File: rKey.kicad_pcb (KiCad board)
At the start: 2 copper layers, 52.8 x 71.4 mm, 39 parts, among them IC1 BDX34C, J1 Conn_01x06, Q1 BC337, Q2 BC337, Q3 BC337, Q4 BC337, Q5 BC327, Q8 BC337, U1 TL084BCN, U2 LM7810_TO220

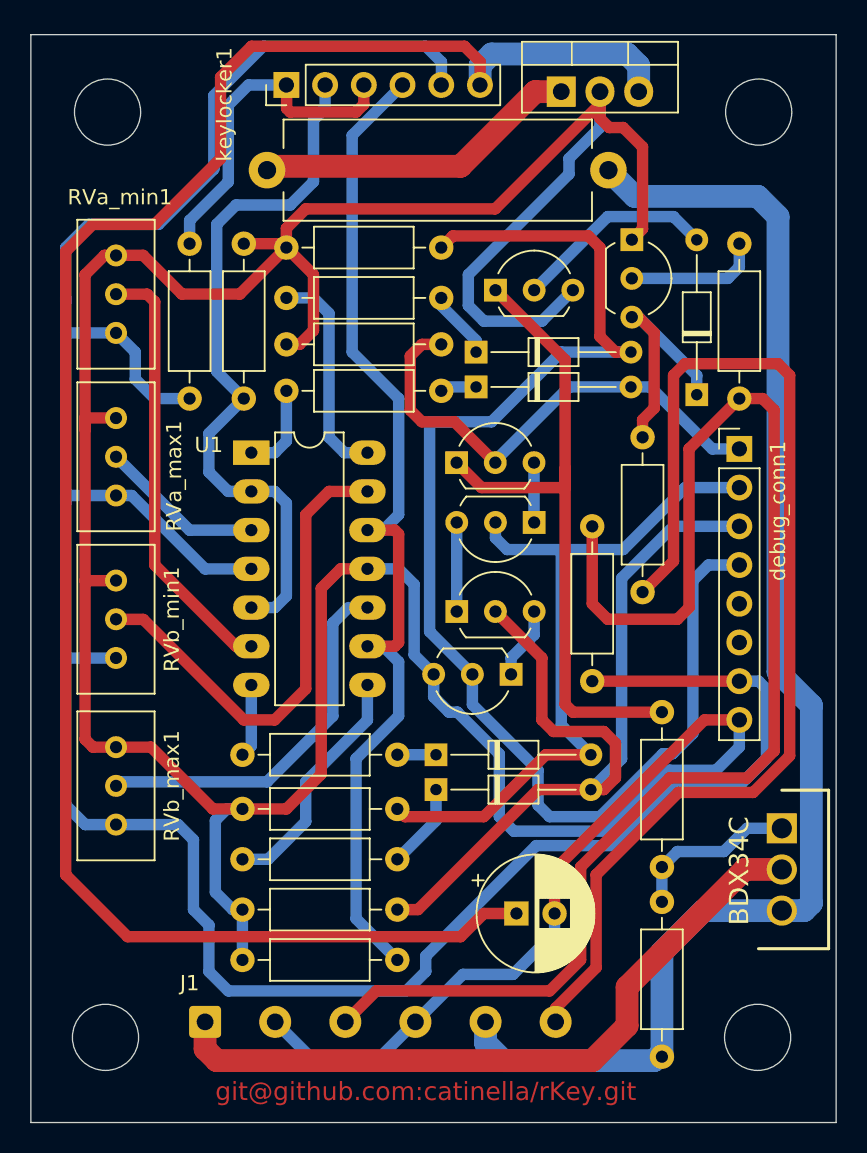
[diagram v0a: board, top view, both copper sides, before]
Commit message: feat: Locking the engine when the vehicle is off
In order to forbid to manually run the engine when the vehicle is off, I added a NC micro relay.
PCB size has been reduced
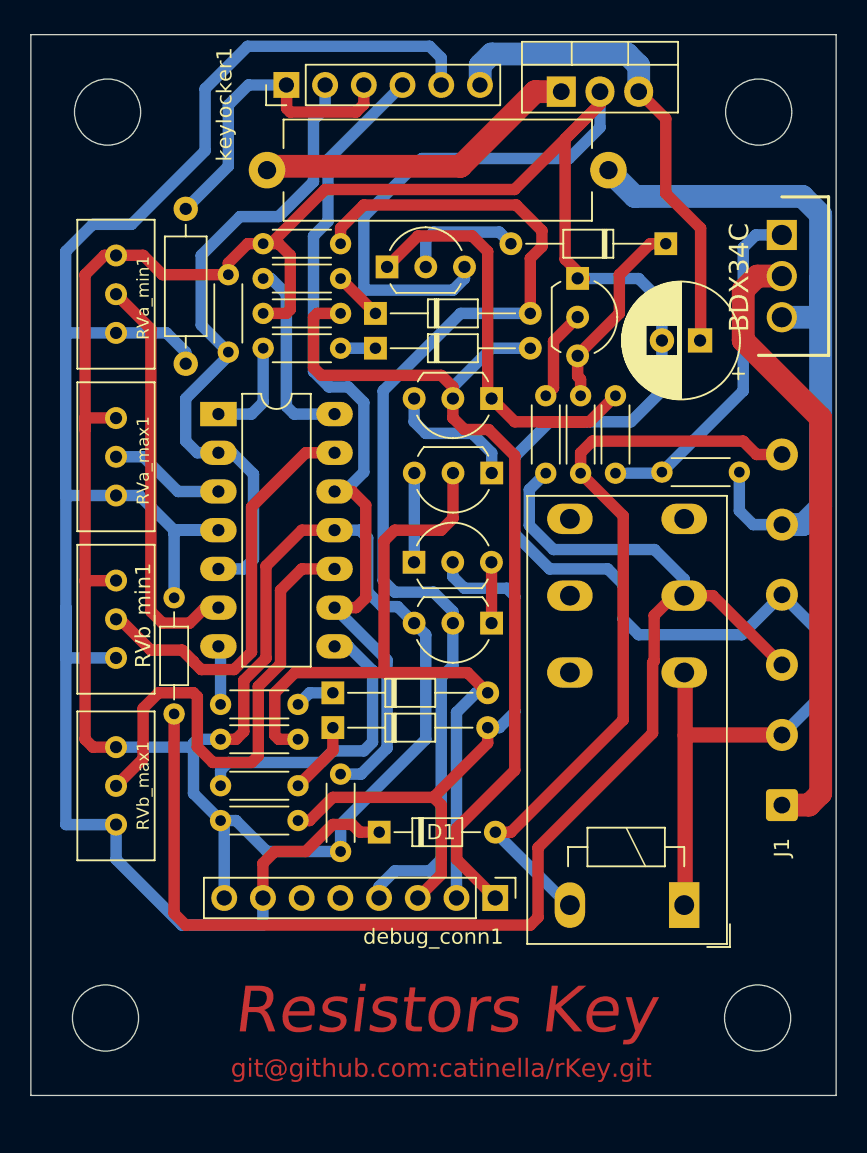
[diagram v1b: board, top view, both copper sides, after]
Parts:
- added D1: DIODE, Diode_THT:D_DO-34_SOD68_P7.62mm_Horizontal, F.Cu at (139.4, 109.0)
- added K1: RT42xxxx, Relay_THT:Relay_DPDT_Schrack-RT2-FormC_RM5mm, F.Cu at (159.5, 113.8)
- R10, R11, R12, R13, R15, R16, R17, R2, R3, R4, R5, R7, R8, R9: footprint Resistor_THT:R_Axial_DIN0207_L6.3mm_D2.5mm_P10.16mm_Horizontal -> Resistor_THT:R_Axial_DIN0204_L3.6mm_D1.6mm_P5.08mm_Horizontal
- R14: footprint Resistor_THT:R_Axial_DIN0207_L6.3mm_D2.5mm_P10.16mm_Horizontal -> Resistor_THT:R_Axial_DIN0204_L3.6mm_D1.6mm_P7.62mm_Horizontal
- moved J1 40.4 mm to (165.9, 107.2), turned to 90 degrees
- moved C1 39.5 mm to (160.5, 76.7), turned to 180 degrees
- moved IC1 38.9 mm to (165.9, 69.8)
- moved debug_conn1 33.5 mm to (147.1, 113.3), turned to -90 degrees
- moved R11 28.2 mm to (158.0, 85.3), turned to 0 degrees
- moved R14 28.0 mm to (126.0, 93.6), turned to -90 degrees
- moved R10 21.0 mm to (154.9, 80.3)
- moved R13 16.1 mm to (150.4, 80.3)
- moved R8 12.7 mm to (136.9, 105.2), turned to -90 degrees
- moved ZD1 10.1 mm to (158.2, 70.4), turned to 180 degrees
- moved ZD2 7.90 mm to (136.4, 99.8)
- moved ZD3 7.90 mm to (136.4, 102.1)
- moved Q8 7.27 mm to (140.0, 71.9)
- moved ZD5 7.08 mm to (139.2, 77.2)
- moved ZD4 7.08 mm to (139.2, 74.9)
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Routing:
- net Net-(U2-Pad3): track 124.1 -> 31.8 mm
- net Net-(R1-Pad1): track 179.0 -> 136.1 mm
- net Net-(IC1-Pad3): track 89.7 -> 48.1 mm
- net GND: track 256.8 -> 289.2 mm
- net Net-(Q1-Pad2): track 32.7 -> 60.5 mm
- net Net-(K1-PadA2): track 75.0 -> 50.8 mm
- net Net-(Q3-Pad2): track 57.8 -> 38.4 mm
- net Net-(Q4-Pad2): track 88.8 -> 73.1 mm
- net Net-(Q1-Pad1): track 44.7 -> 30.1 mm
- net Net-(IC1-Pad1): track 10.7 -> 22.1 mm
- net Net-(R8-Pad1): track 69.0 -> 57.6 mm
- net Net-(RVb_max1-Pad2): track 23.7 -> 33.8 mm
- net Net-(IC1-Pad2): track 46.6 -> 40.9 mm
- net Net-(Q8-Pad2): track 13.3 -> 7.89 mm
- net Net-(Q1-Pad3): track 3.93 -> 8.78 mm
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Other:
- board size 52.8 x 71.4 mm -> 52.8 x 69.6 mm
- board text added: "Resistors Key"

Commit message: small fixes...
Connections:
- J1 pad 3: Net-(K1-Pad11) -> Net-(J1-Pad3)
- K1 pad 11: Net-(K1-Pad11) -> Net-(J1-Pad3)
- K1 pad 21: unconnected-(K1-Pad21) -> Net-(J1-Pad3)
- K1 pad 22: unconnected-(K1-Pad22) -> GND
- R13 pad 2: Net-(K1-Pad11) -> Net-(J1-Pad3)
- R14 pad 2: Net-(K1-Pad11) -> Net-(J1-Pad3)
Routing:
- net Net-(J1-Pad3): track 0.00 -> 88.1 mm
- net Net-(K1-Pad11): track 87.9 -> 0.00 mm
- net GND: track 289.2 -> 293.8 mm

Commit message: fixes
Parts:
- removed D1: DIODE, Diode_THT:D_DO-34_SOD68_P7.62mm_Horizontal
- added C2: 150uF, Capacitor_THT:CP_Radial_D7.5mm_P2.50mm, F.Cu at (131.1, 121.6)
- added Q6: BC327, Package_TO_SOT_THT:TO-92L_Inline_Wide, F.Cu at (151.6, 118.6)
- added Q7: BC337, Package_TO_SOT_THT:TO-92L_Inline_Wide, F.Cu at (138.2, 121.9)
- added Q9: BC327, Package_TO_SOT_THT:TO-92L_Inline_Wide, F.Cu at (153.9, 119.6)
- added R18: 50K, Resistor_THT:R_Axial_DIN0204_L3.6mm_D1.6mm_P5.08mm_Horizontal, F.Cu at (136.4, 125.0)
- added R19: 20K, Resistor_THT:R_Axial_DIN0204_L3.6mm_D1.6mm_P5.08mm_Horizontal, F.Cu at (149.1, 125.0)
- added R20: 20K, Resistor_THT:R_Axial_DIN0204_L3.6mm_D1.6mm_P5.08mm_Horizontal, F.Cu at (151.4, 125.0)
- added R21: 200K, Resistor_THT:R_Axial_DIN0204_L3.6mm_D1.6mm_P5.08mm_Horizontal, F.Cu at (138.2, 117.9)
- added R22: 10K, Resistor_THT:R_Axial_DIN0204_L3.6mm_D1.6mm_P5.08mm_Horizontal, F.Cu at (156.5, 122.7)
- moved J1 4.81 mm to (164.6, 111.8)
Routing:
- net Net-(R14-Pad1): track 136.1 -> 164.9 mm
- net Net-(C2-Pad1): track 0.00 -> 22.9 mm
- net Net-(R13-Pad2): track 88.1 -> 109.5 mm
- net Net-(Q7-Pad1): track 0.00 -> 15.3 mm
- net Net-(J1-Pad6): track 50.8 -> 61.6 mm
- net Net-(Q9-Pad3): track 0.00 -> 6.44 mm
- net Net-(Q6-Pad2): track 0.00 -> 6.35 mm
- net Net-(IC1-Pad2): track 40.9 -> 46.6 mm
- net Net-(IC1-Pad3): track 48.1 -> 51.9 mm
- net Net-(Q7-Pad2): track 0.00 -> 3.43 mm
- net Net-(R10-Pad1): track 30.1 -> 26.8 mm
- net Net-(Q9-Pad2): track 0.00 -> 3.11 mm
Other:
- board text removed: "Resistors Key"

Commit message: fix
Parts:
- removed R6: 20, Resistor_THT:R_Axial_Power_L20.0mm_W6.4mm_P22.40mm
- R1: footprint Resistor_THT:R_Axial_DIN0207_L6.3mm_D2.5mm_P10.16mm_Horizontal -> Resistor_THT:R_Axial_Power_L20.0mm_W6.4mm_P22.40mm
- U2: value LM7810_TO220 -> LM7810
- moved R1 28.0 mm to (151.7, 65.5), turned to 180 degrees
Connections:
- IC1 pad 3: Net-(IC1-Pad3) -> Net-(U2-Pad1)
- J1 pad 5: Net-(IC1-Pad3) -> Net-(U2-Pad1)
- R11 pad 2: Net-(IC1-Pad3) -> Net-(U2-Pad1)
- U2 pad 1: Net-(R6-Pad1) -> Net-(U2-Pad1)
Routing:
- net Net-(U2-Pad1): track 0.00 -> 57.6 mm
- net Net-(IC1-Pad3): track 51.9 -> 0.00 mm
- net GND: track 293.7 -> 272.0 mm, vias 0 -> 1
- net Net-(R6-Pad1): track 21.4 -> 0.00 mm
- net Net-(Q6-Pad3): track 164.9 -> 172.8 mm
- net Net-(R1-Pad2): track 20.8 -> 17.2 mm

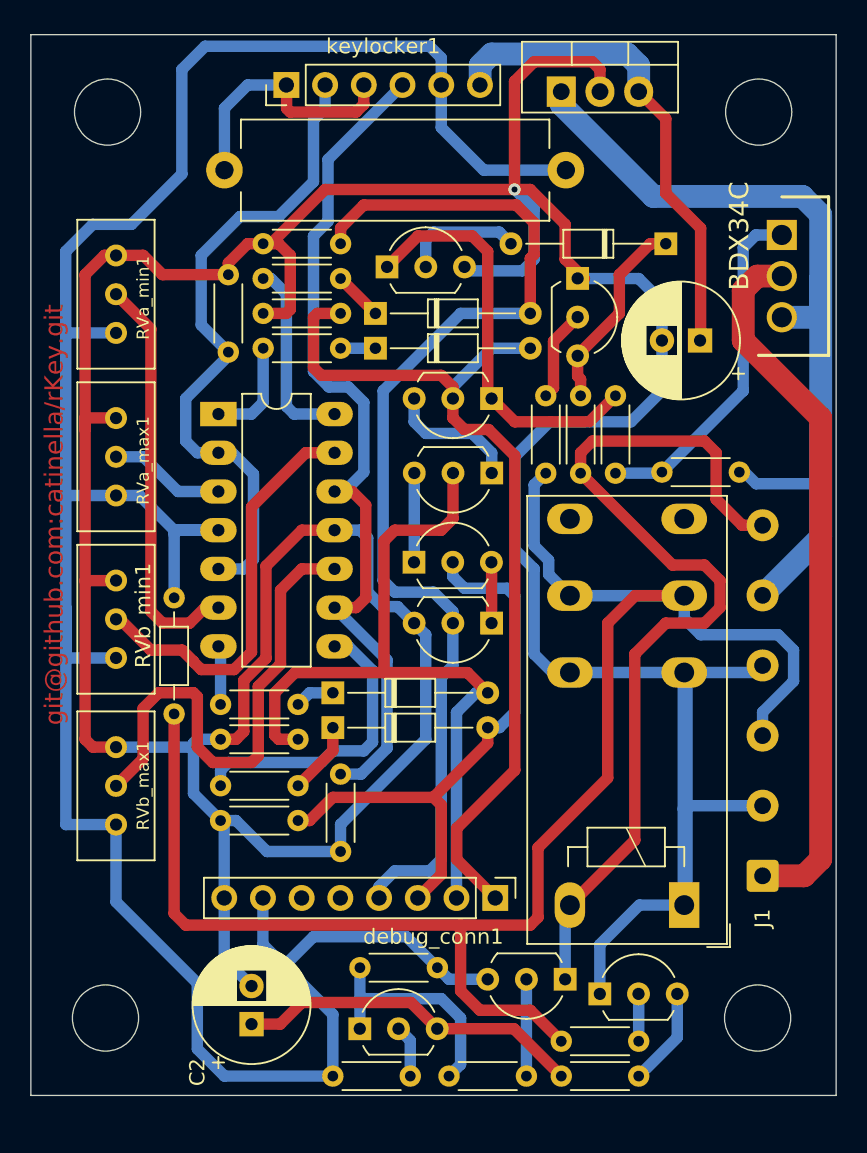
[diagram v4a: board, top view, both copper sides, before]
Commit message: Enhancements and fixes
1) the generic rerlay has been replaced by HK19F
2) unuseful components have been removed
3) pull-down resistors resizing from 8K to more common 10K
4) the 12K resistor linked to the BC237 IC's emiotter, has been resized from 12K to 6K
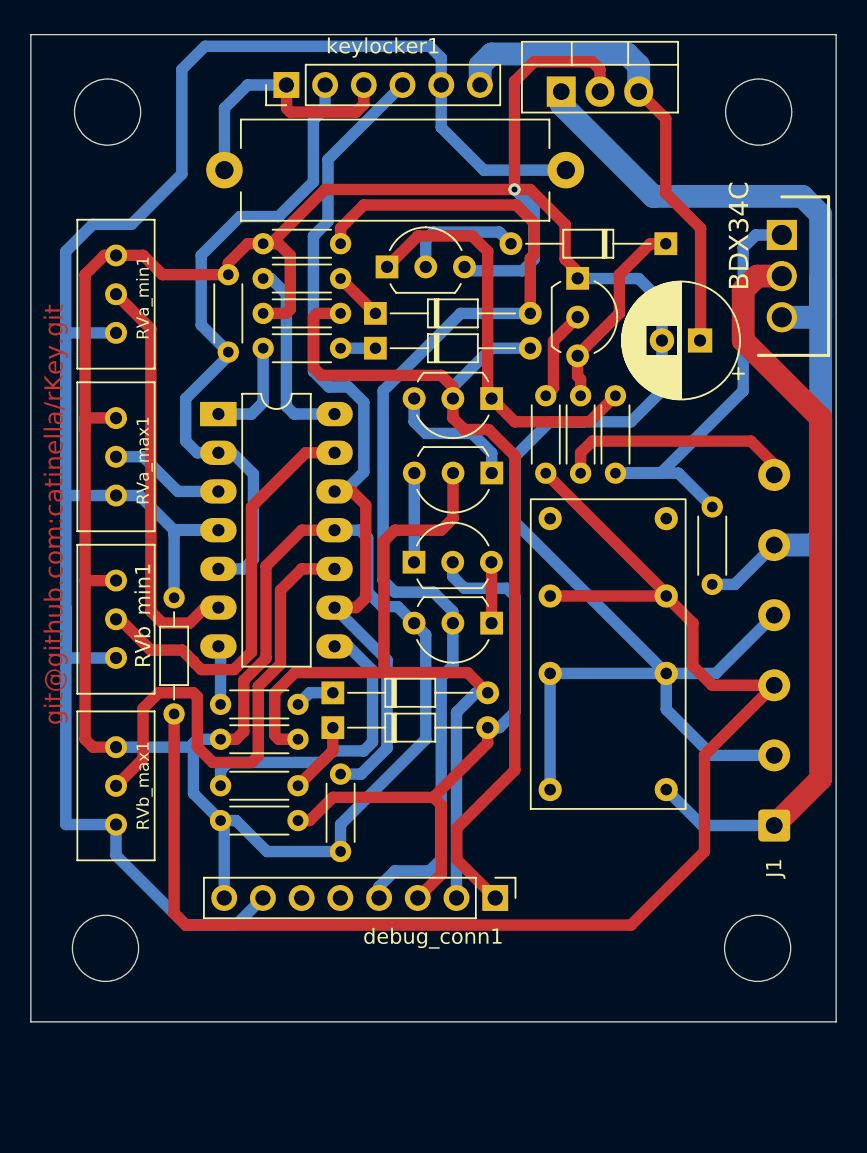
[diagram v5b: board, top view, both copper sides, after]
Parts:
- removed C2: 150uF, Capacitor_THT:CP_Radial_D7.5mm_P2.50mm
- removed K1: RT42xxxx, Relay_THT:Relay_DPDT_Schrack-RT2-FormC_RM5mm
- removed Q6, Q9: BC327, Package_TO_SOT_THT:TO-92L_Inline_Wide
- removed Q7: BC337, Package_TO_SOT_THT:TO-92L_Inline_Wide
- removed R18: 50K, Resistor_THT:R_Axial_DIN0204_L3.6mm_D1.6mm_P5.08mm_Horizontal
- removed R19, R20: 20K, Resistor_THT:R_Axial_DIN0204_L3.6mm_D1.6mm_P5.08mm_Horizontal
- removed R21: 200K, Resistor_THT:R_Axial_DIN0204_L3.6mm_D1.6mm_P5.08mm_Horizontal
- removed R22: 10K, Resistor_THT:R_Axial_DIN0204_L3.6mm_D1.6mm_P5.08mm_Horizontal
- added U3: HK19F-DC12-SHG, HK19F:HK19F-DC12-SHG, F.Cu at (160.8, 98.6)
- R12, R15, R16, R17: value 8K -> 10K
- R9: value 12K -> 6K
- U2: value LM7810 -> LM7810_TO220
- moved R11 4.02 mm to (161.3, 87.6), turned to -90 degrees
- moved J1 3.39 mm to (165.4, 108.5)
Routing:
- net Net-(J1-Pad6): track 61.6 -> 15.7 mm
- net Net-(R1-Pad1): track 172.8 -> 131.7 mm
- net Net-(C2-Pad1): track 22.9 -> 0.00 mm
- net Net-(J1-Pad3): track 109.5 -> 93.1 mm
- net Net-(Q7-Pad1): track 15.3 -> 0.00 mm
- net GND: track 272.0 -> 259.1 mm
- net Net-(IC1-Pad1): track 22.1 -> 29.4 mm
- net Net-(Q9-Pad3): track 6.44 -> 0.00 mm
- net Net-(Q6-Pad2): track 6.35 -> 0.00 mm
- net Net-(Q7-Pad2): track 3.43 -> 0.00 mm
- net Net-(Q9-Pad2): track 3.11 -> 0.00 mm
- net Net-(IC1-Pad2): track 46.6 -> 49.5 mm
- net Net-(IC1-Pad3): track 57.6 -> 55.5 mm
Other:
- board size 52.8 x 69.6 mm -> 52.8 x 64.8 mm
